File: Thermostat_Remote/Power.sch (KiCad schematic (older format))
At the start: 0 parts

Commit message: Update remote sensor layout
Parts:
- added BT1, BT2: BATTERY-20MM_SMD, Battery:BatteryHolder_Keystone_3034_1x20mm, symbol SparkFun-Batteries:BATTERY-20MM_SMD
- added C11, C14: 1uF, Capacitor_SMD:C_0402_1005Metric, symbol Device:C
- added C12, C13: 0.1uF, Capacitor_SMD:C_0402_1005Metric, symbol Device:C
- added R8: 220kΩ, Resistors:0402, symbol Device:R_US
- added R9: 100kΩ, Resistors:0402, symbol Device:R_US
- added U5: TSR_1-2433, Converter_DCDC:Converter_DCDC_TRACO_TSR-1_THT, symbol Regulator_Switching:TSR_1-2433
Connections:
- new net: BT1.2 (-), BT2.1 (+)
- new net 3.3V: C13.1, C14.1, U5.3 (Vout)
- new net BATT_MON: R8.2, R9.1
- new net GND: BT2.2 (-), C11.2, C12.2, C13.2, C14.2, R9.2, U5.2 (GND)
- new net V_BATT: BT1.1 (+), C11.1, C12.1, R8.1, U5.1 (Vin)
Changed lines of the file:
@@
 Comment4 ""
 $EndDescr
+$Comp
+L SparkFun-Batteries:BATTERY-20MM_SMD BT1
+U 1 1 5D51775D
+P 3550 2400
+F 0 "BT1" V 3455 2578 45  0000 L CNN
+F 1 "BATTERY-20MM_SMD" V 3539 2578 45  0000 L CNN
+F 2 "Battery:BatteryHolder_Keystone_3034_1x20mm" H 3550 2650 20  0001 C CNN
+F 3 "" H 3550 2400 50  0001 C CNN
+F 4 "BATT-11519" V 3634 2578 60  0000 L CNN "Field4"
+	1    3550 2400
+	0    1    1    0
+$EndComp
+$Comp
+L SparkFun-Batteries:BATTERY-20MM_SMD BT2
+U 1 1 5D518681
+P 3550 2950
+F 0 "BT2" V 3455 3128 45  0000 L CNN
+F 1 "BATTERY-20MM_SMD" V 3539 3128 45  0000 L CNN
+F 2 "Battery:BatteryHolder_Keystone_3034_1x20mm" H 3550 3200 20  0001 C CNN
+F 3 "" H 3550 2950 50  0001 C CNN
+F 4 "BATT-11519" V 3634 3128 60  0000 L CNN "Field4"
+	1    3550 2950
+	0    1    1    0
+$EndComp
+Wire Wire Line
+	3550 2750 3550 2600
+$Comp
+L Regulator_Switching:TSR_1-2433 U5
+U 1 1 5D5193D4
+P 6000 2300
+F 0 "U5" H 6000 2667 50  0000 C CNN
+F 1 "TSR_1-2433" H 6000 2576 50  0000 C CNN
+F 2 "Converter_DCDC:Converter_DCDC_TRACO_TSR-1_THT" H 6000 2150 50  0001 L CIN
+F 3 "http://www.tracopower.com/products/tsr1.pdf" H 6000 2300 50  0001 C CNN
+	1    6000 2300
+	1    0    0    -1
+$EndComp
+$Comp
+L Device:C C11
+U 1 1 5D51B6DD
+P 4650 2700
+F 0 "C11" H 4765 2746 50  0000 L CNN
+F 1 "1uF" H 4765 2655 50  0000 L CNN
+F 2 "Capacitor_SMD:C_0402_1005Metric" H 4688 2550 50  0001 C CNN
+F 3 "~" H 4650 2700 50  0001 C CNN
+	1    4650 2700
+	1    0    0    -1
+$EndComp
+$Comp
+L Device:C C12
+U 1 1 5D51D2D7
+P 5200 2700
+F 0 "C12" H 5315 2746 50  0000 L CNN
+F 1 "0.1uF" H 5315 2655 50  0000 L CNN
+F 2 "Capacitor_SMD:C_0402_1005Metric" H 5238 2550 50  0001 C CNN
+F 3 "~" H 5200 2700 50  0001 C CNN
+	1    5200 2700
+	1    0    0    -1
+$EndComp
+Wire Wire Line
+	3550 2200 4650 2200
+Wire Wire Line
+	4650 2550 4650 2200
+Connection ~ 4650 2200
+Wire Wire Line
+	4650 2200 5200 2200
+Wire Wire Line
+	5200 2550 5200 2200
+Connection ~ 5200 2200
+Wire Wire Line
+	5200 2200 5600 2200
+Wire Wire Line
+	3550 3150 3550 3300
+Wire Wire Line
+	3550 3300 4650 3300
+Wire Wire Line
+	4650 3300 4650 2850
+Wire Wire Line
+	4650 3300 5200 3300
+Wire Wire Line
+	5200 3300 5200 2850
+Connection ~ 4650 3300
+Wire Wire Line
+	6000 2500 6000 3300
+Wire Wire Line
+	6000 3300 5200 3300
+Connection ~ 5200 3300
+$Comp
+L Device:C C13
+U 1 1 5D520C47
+P 6700 2700
+F 0 "C13" H 6815 2746 50  0000 L CNN
+F 1 "0.1uF" H 6815 2655 50  0000 L CNN
+F 2 "Capacitor_SMD:C_0402_1005Metric" H 6738 2550 50  0001 C CNN
+F 3 "~" H 6700 2700 50  0001 C CNN
+	1    6700 2700
+	1    0    0    -1
+$EndComp
+$Comp
+L Device:C C14
+U 1 1 5D521ABD
+P 7200 2700
+F 0 "C14" H 7315 2746 50  0000 L CNN
+F 1 "1uF" H 7315 2655 50  0000 L CNN
+F 2 "Capacitor_SMD:C_0402_1005Metric" H 7238 2550 50  0001 C CNN
+F 3 "~" H 7200 2700 50  0001 C CNN
+	1    7200 2700
+	1    0    0    -1
+$EndComp
+Wire Wire Line
+	6400 2200 6700 2200
+Wire Wire Line
+	6700 2200 6700 2550
+Wire Wire Line
+	6700 2200 7200 2200
+Wire Wire Line
+	7200 2200 7200 2550
+Connection ~ 6700 2200
+Wire Wire Line
+	6000 3300 6700 3300
+Wire Wire Line
+	6700 3300 6700 2850
+Connection ~ 6000 3300
+Wire Wire Line
+	6700 3300 7200 3300
+Wire Wire Line
+	7200 3300 7200 2850
+Connection ~ 6700 3300
+$Comp
+L SparkFun-PowerSymbols:3.3V #SUPPLY0108
+U 1 1 5D522CA7
+P 7200 2200
+F 0 "#SUPPLY0108" H 7250 2200 45  0001 L BNN
+F 1 "3.3V" H 7200 2476 45  0000 C CNN
+F 2 "XXX-00000" H 7200 2381 60  0000 C CNN
+F 3 "" H 7200 2200 60  0001 C CNN
+	1    7200 2200
+	1    0    0    -1
+$EndComp
+Connection ~ 7200 2200
+$Comp
+L SparkFun-PowerSymbols:GND #GND0115
+U 1 1 5D523187
+P 6000 3300
+F 0 "#GND0115" H 6050 3250 45  0001 L BNN
+F 1 "GND" H 6000 3130 45  0000 C CNN
+F 2 "" H 6000 3200 60  0001 C CNN
+F 3 "" H 6000 3200 60  0001 C CNN
+	1    6000 3300
+	1    0    0    -1
+$EndComp
+$Comp
+L SparkFun-PowerSymbols:V_BATT #SUPPLY0109
+U 1 1 5D523690
+P 4650 2200
+F 0 "#SUPPLY0109" H 4700 2200 45  0001 L BNN
+F 1 "V_BATT" H 4650 2476 45  0000 C CNN
+F 2 "XXX-00000" H 4650 2381 60  0000 C CNN
+F 3 "" H 4650 2200 60  0001 C CNN
+	1    4650 2200
+	1    0    0    -1
+$EndComp
+$Comp
+L SparkFun-PowerSymbols:V_BATT #SUPPLY0110
+U 1 1 5D528E0A
+P 4700 4300
+F 0 "#SUPPLY0110" H 4750 4300 45  0001 L BNN
+F 1 "V_BATT" H 4700 4576 45  0000 C CNN
+F 2 "XXX-00000" H 4700 4481 60  0000 C CNN
+F 3 "" H 4700 4300 60  0001 C CNN
+	1    4700 4300
+	1    0    0    -1
+$EndComp
+$Comp
+L Device:R_US R8
+U 1 1 5D529579
+P 4700 4450
+F 0 "R8" H 4768 4496 50  0000 L CNN
+F 1 "220kΩ" H 4768 4405 50  0000 L CNN
+F 2 "Resistors:0402" V 4740 4440 50  0001 C CNN
+F 3 "~" H 4700 4450 50  0001 C CNN
+	1    4700 4450
+	1    0    0    -1
+$EndComp
+$Comp
+L Device:R_US R9
+U 1 1 5D529C92
+P 4700 4750
+F 0 "R9" H 4768 4796 50  0000 L CNN
+F 1 "100kΩ" H 4768 4705 50  0000 L CNN
+F 2 "Resistors:0402" V 4740 4740 50  0001 C CNN
+F 3 "~" H 4700 4750 50  0001 C CNN
+	1    4700 4750
+	1    0    0    -1
+$EndComp
+$Comp
+L SparkFun-PowerSymbols:GND #GND0116
+U 1 1 5D52A1D6
+P 4700 4900
+F 0 "#GND0116" H 4750 4850 45  0001 L BNN
+F 1 "GND" H 4700 4730 45  0000 C CNN
+F 2 "" H 4700 4800 60  0001 C CNN
+F 3 "" H 4700 4800 60  0001 C CNN
+	1    4700 4900
+	1    0    0    -1
+$EndComp
+Wire Wire Line
+	4700 4600 5300 4600
+Connection ~ 4700 4600
+Text GLabel 5300 4600 2    50   Output ~ 0
+BATT_MON
 $EndSCHEMATC

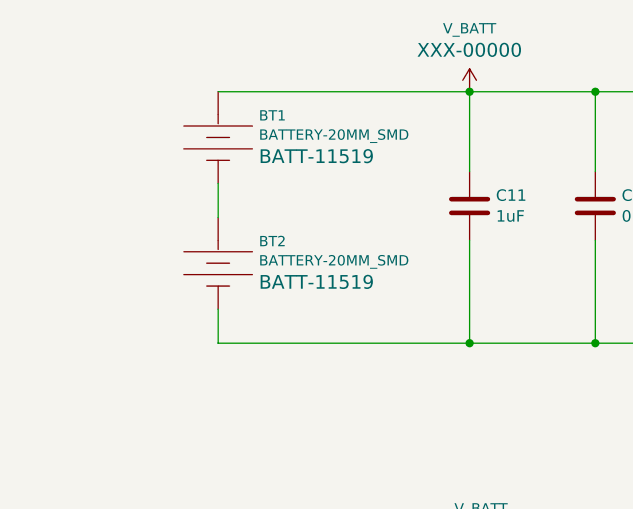
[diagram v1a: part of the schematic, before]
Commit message: Update processor pin definitions
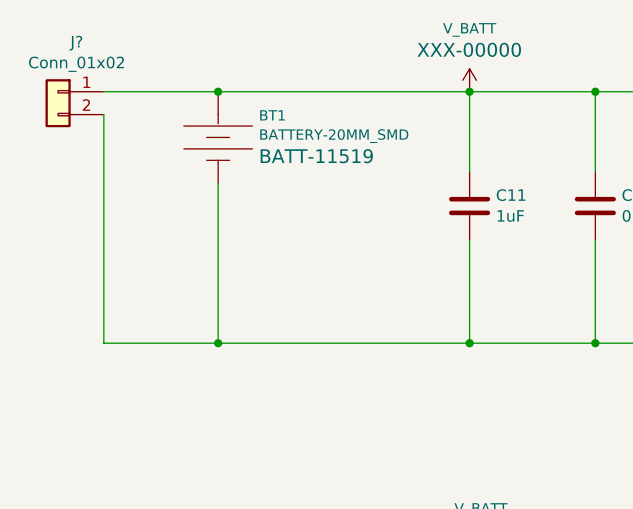
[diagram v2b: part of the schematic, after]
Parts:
- removed BT2: BATTERY-20MM_SMD, Battery:BatteryHolder_Keystone_3034_1x20mm, symbol SparkFun-Batteries:BATTERY-20MM_SMD
- added J?: Conn_01x02, Connector_JST:JST_PH_S2B-PH-SM4-TB_1x02-1MP_P2.00mm_Horizontal, symbol Connector_Generic:Conn_01x02
- BT1: footprint Battery:BatteryHolder_Keystone_3034_1x20mm -> Batteries:BATTCON_20MM
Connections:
- net GND: now also BT1.2 (-), J?.2 (Pin_2)
- net V_BATT: now also J?.1 (Pin_1)
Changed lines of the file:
@@
 $EndDescr
-$Comp
-L SparkFun-Batteries:BATTERY-20MM_SMD BT1
-U 1 1 5D51775D
-P 3550 2400
-F 0 "BT1" V 3455 2578 45  0000 L CNN
-F 1 "BATTERY-20MM_SMD" V 3539 2578 45  0000 L CNN
-F 2 "Battery:BatteryHolder_Keystone_3034_1x20mm" H 3550 2650 20  0001 C CNN
-F 3 "" H 3550 2400 50  0001 C CNN
-F 4 "BATT-11519" V 3634 2578 60  0000 L CNN "Field4"
-	1    3550 2400
-	0    1    1    0
-$EndComp
-$Comp
-L SparkFun-Batteries:BATTERY-20MM_SMD BT2
-U 1 1 5D518681
-P 3550 2950
-F 0 "BT2" V 3455 3128 45  0000 L CNN
-F 1 "BATTERY-20MM_SMD" V 3539 3128 45  0000 L CNN
-F 2 "Battery:BatteryHolder_Keystone_3034_1x20mm" H 3550 3200 20  0001 C CNN
-F 3 "" H 3550 2950 50  0001 C CNN
-F 4 "BATT-11519" V 3634 3128 60  0000 L CNN "Field4"
-	1    3550 2950
-	0    1    1    0
-$EndComp
-Wire Wire Line
-	3550 2750 3550 2600
 $Comp
 L Regulator_Switching:TSR_1-2433 U5
@@
 	5200 2200 5600 2200
 Wire Wire Line
-	3550 3150 3550 3300
-Wire Wire Line
 	3550 3300 4650 3300
 Wire Wire Line
@@
 Text GLabel 5300 4600 2    50   Output ~ 0
 BATT_MON
+$Comp
+L SparkFun-Batteries:BATTERY-20MM_SMD BT1
+U 1 1 5D51775D
+P 3550 2400
+F 0 "BT1" V 3455 2578 45  0000 L CNN
+F 1 "BATTERY-20MM_SMD" V 3539 2578 45  0000 L CNN
+F 2 "Batteries:BATTCON_20MM" H 3550 2650 20  0001 C CNN
+F 3 "" H 3550 2400 50  0001 C CNN
+F 4 "BATT-11519" V 3634 2578 60  0000 L CNN "Field4"
+	1    3550 2400
+	0    1    1    0
+$EndComp
+Wire Wire Line
+	3550 2600 3550 3300
+$Comp
+L Connector_Generic:Conn_01x02 J?
+U 1 1 5D531177
+P 2850 2200
+F 0 "J?" H 2768 2417 50  0000 C CNN
+F 1 "Conn_01x02" H 2768 2326 50  0000 C CNN
+F 2 "Connector_JST:JST_PH_S2B-PH-SM4-TB_1x02-1MP_P2.00mm_Horizontal" H 2850 2200 50  0001 C CNN
+F 3 "~" H 2850 2200 50  0001 C CNN
+	1    2850 2200
+	-1   0    0    -1
+$EndComp
+Wire Wire Line
+	3050 2200 3550 2200
+Connection ~ 3550 2200
+Wire Wire Line
+	3050 2300 3050 3300
+Wire Wire Line
+	3050 3300 3550 3300
+Connection ~ 3550 3300
 $EndSCHEMATC
